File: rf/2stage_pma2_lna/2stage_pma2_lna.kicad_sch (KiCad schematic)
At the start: 26 parts, among them J1 SMA, J2 SMA, U1 PMA2-43LN+, U2 PMA2-63LN+, X1 SAW, X2 SAW

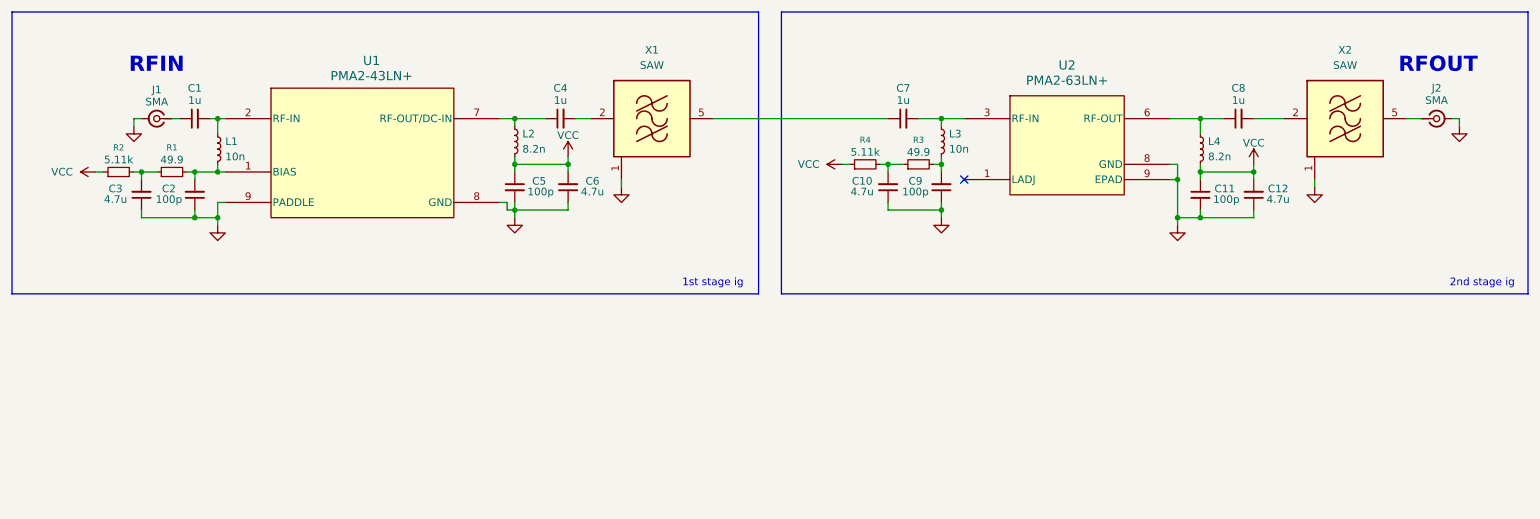
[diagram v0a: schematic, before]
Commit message: Update gitignore and PMA2 based LNA files
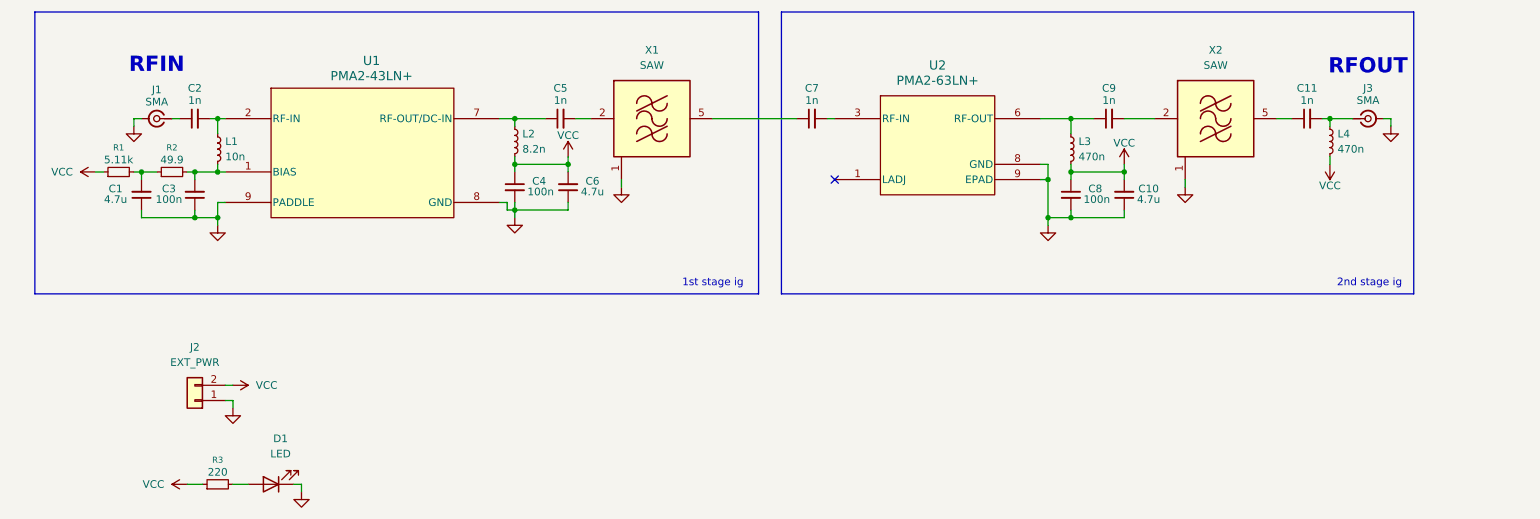
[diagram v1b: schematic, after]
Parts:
- removed C1, C4: 1u, Capacitor_SMD:C_0603_1608Metric_Pad1.08x0.95mm_HandSolder, symbol Device:C_Small
- removed C10: 4.7u, Capacitor_SMD:C_0603_1608Metric_Pad1.08x0.95mm_HandSolder, symbol Device:C_Small
- removed C9: 100p, Capacitor_SMD:C_0603_1608Metric_Pad1.08x0.95mm_HandSolder, symbol Device:C_Small
- removed L3: 10n, Inductor_SMD:L_0603_1608Metric_Pad1.05x0.95mm_HandSolder, symbol Device:L_Small
- removed R4: 5.11k, Resistor_SMD:R_0603_1608Metric_Pad0.98x0.95mm_HandSolder, symbol Device:R_Small
- added C11, C2, C5: 1n, Capacitor_SMD:C_0603_1608Metric_Pad1.08x0.95mm_HandSolder, symbol Device:C_Small
- added D1: LED, LED_THT:LED_D5.0mm_Clear, symbol Device:LED
- added J2: EXT_PWR, Connector_PinHeader_2.54mm:PinHeader_1x02_P2.54mm_Vertical, symbol Connector_Generic:Conn_01x02
- added L4: 470n, Inductor_SMD:L_0603_1608Metric_Pad1.05x0.95mm_HandSolder, symbol Device:L_Small
- C3: renamed from C2; value 100p -> 100n
- C4: renamed from C5; value 100p -> 100n
- C7: value 1u -> 1n
- C8: renamed from C11; value 100p -> 100n
- C9: renamed from C8; value 1u -> 1n
- L3: renamed from L4; value 8.2n -> 470n
- R3: value 49.9 -> 220
- renumbered C3 to C1, C12 to C10, J2 to J3, R2 to R1, R1 to R2
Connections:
- net GND: now also D1.1 (K), J2.1 (Pin_1)
- net VCC: now also R3.1, J2.2 (Pin_2), L4.2
- net at L1.1, U1.2 (RF-IN): now also C2.2
- net at X2.5 (OUT): now also C11.1; no longer J3.1 (In)
- net at J1.1 (In): now also C2.1
- net at L2.1, U1.7 (RF-OUT/DC-IN): now also C5.1
- net at R3.2: now also D1.2 (A)
- net at X1.2 (IN): now also C5.2
- new net: C11.2, J3.1 (In), L4.1
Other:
- moved on the sheet: C10, C8, C9, J3, L3, U2, X2
